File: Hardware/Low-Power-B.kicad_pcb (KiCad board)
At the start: 2 copper layers, 55.2 x 40.6 mm, 25 parts, among them J1 01x02, Q1 BC557, Q2 BC547, Q3 BC557, Q4 BC547, Q5 BC547, U1 Arduino_Pro_Micro, U2 VS1838B

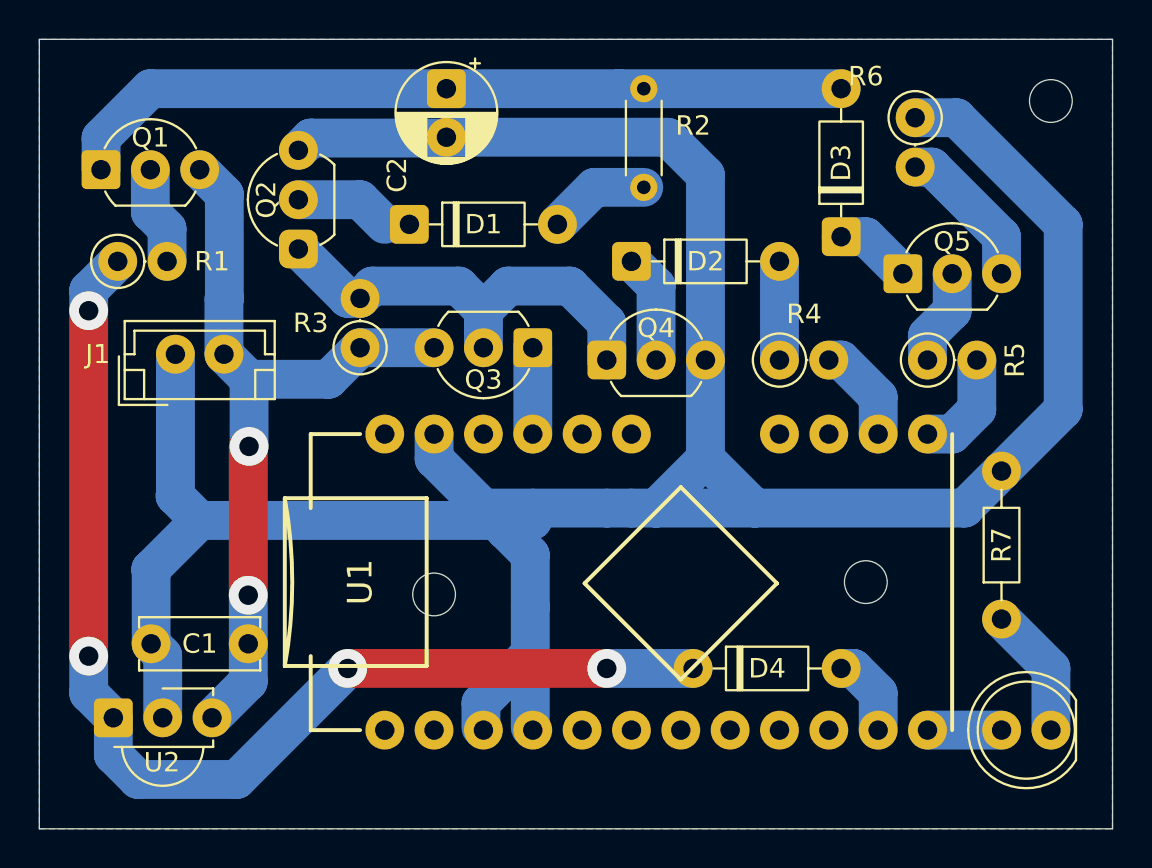
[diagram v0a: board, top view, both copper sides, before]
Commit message: Adding Low-Power-B 3D model
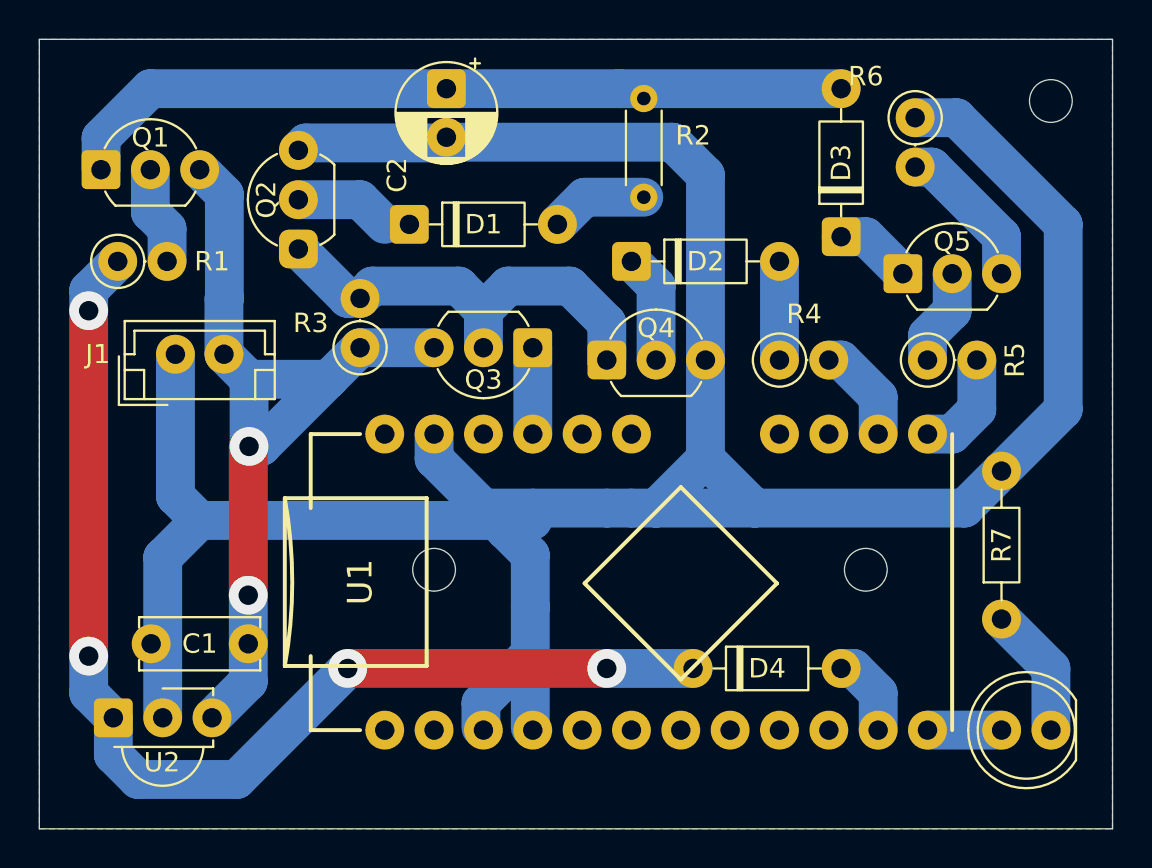
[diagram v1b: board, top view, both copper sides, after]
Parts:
- moved H2 1.27 mm to (162.6, 78.1)
- moved H3 0.63 mm to (184.8, 78.1)
- moved R2 0.51 mm to (173.4, 58.9)
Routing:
- net +5V: track 40.3 -> 45.8 mm
- net GND: track 154.8 -> 153.9 mm
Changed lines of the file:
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@@
 	(footprint "MountingHole:MountingHole_2.2mm_M2_ISO7380"
 		(layer "F.Cu")
-		(at 184.785 78.74)
+		(at 184.785 78.105)
 		(descr "Mounting Hole 2.2mm, M2, no annular, generated by kicad-footprint-generator mountinghole.py")
 		(tags "mountinghole M2 ISO7380")
@@
 	(footprint "Resistor_THT:R_Axial_DIN0204_L3.6mm_D1.6mm_P5.08mm_Horizontal"
 		(layer "F.Cu")
-		(at 173.355 58.42 90)
+		(at 173.355 58.928 90)
 		(descr "Resistor, Axial_DIN0204 series, Axial, Horizontal, pin pitch=5.08mm, 0.167W, length*diameter=3.6*1.6mm^2, http://cdn-reichelt.de/documents/datenblatt/B400/1_4W%23YAG.pdf")
 		(tags "Resistor Axial_DIN0204 series Axial Horizontal pin pitch 5.08mm 0.167W length 3.6mm diameter 1.6mm")
@@
 	(footprint "MountingHole:MountingHole_2.2mm_M2_ISO7380"
 		(layer "F.Cu")
-		(at 162.56 79.375)
+		(at 162.56 78.105)
 		(descr "Mounting Hole 2.2mm, M2, no annular, generated by kicad-footprint-generator mountinghole.py")
 		(tags "mountinghole M2 ISO7380")
@@
 	)
 	(segment
-		(start 147.995 81.915)
-		(end 147.995 78.105)
+		(start 163.195 56.094)
+		(end 174.839 56.094)
+		(width 2)
+		(layer "B.Cu")
+		(net 1)
+	)
+	(segment
+		(start 148.59 77.47)
+		(end 150.495 75.565)
+		(width 2)
+		(layer "B.Cu")
+		(net 1)
+	)
+	(segment
+		(start 148.59 85.725)
+		(end 148.59 77.47)
 		(width 2)
 		(layer "B.Cu")
@@
 	)
 	(segment
-		(start 148.59 85.725)
-		(end 148.59 82.51)
-		(width 2)
-		(layer "B.Cu")
-		(net 1)
-	)
-	(segment
-		(start 150.475 75.545)
-		(end 149.225 74.295)
+		(start 149.245 74.315)
+		(end 150.495 75.565)
 		(width 2)
 		(layer "B.Cu")
@@
 	)
 	(segment
-		(start 148.59 82.51)
-		(end 147.995 81.915)
+		(start 149.245 67.01)
+		(end 149.245 74.315)
 		(width 2)
 		(layer "B.Cu")
@@
 	)
 	(segment
-		(start 149.225 74.295)
-		(end 149.245 74.275)
-		(width 2)
-		(layer "B.Cu")
-		(net 1)
-	)
-	(segment
 		(start 164.973 84.963)
 		(end 167.513 82.423)
@@
 	)
 	(segment
-		(start 163.195 55.84)
-		(end 174.585 55.84)
-		(width 2)
-		(layer "B.Cu")
-		(net 1)
-	)
-	(segment
-		(start 156.21 55.88)
-		(end 155.575 56.515)
-		(width 2)
-		(layer "B.Cu")
-		(net 1)
-	)
-	(segment
 		(start 176.53 67.31)
 		(end 176.53 72.39)
@@
 	)
 	(segment
-		(start 147.975 78.085)
-		(end 150.475 75.585)
-		(width 2)
-		(layer "B.Cu")
-		(net 1)
-	)
-	(segment
 		(start 189.455 54.835)
 		(end 194.945 60.325)
@@
 	)
 	(segment
+		(start 167.64 74.93)
+		(end 165.1 74.93)
+		(width 2)
+		(layer "B.Cu")
+		(net 1)
+	)
+	(segment
+		(start 166.243 76.073)
+		(end 167.513 77.343)
+		(width 2)
+		(layer "B.Cu")
+		(net 1)
+	)
+	(segment
+		(start 155.575 56.515)
+		(end 155.956 56.134)
+		(width 2)
+		(layer "B.Cu")
+		(net 1)
+	)
+	(segment
+		(start 176.53 72.39)
+		(end 179.07 74.93)
+		(width 2)
+		(layer "B.Cu")
+		(net 1)
+	)
+	(segment
+		(start 174.839 56.094)
+		(end 176.53 57.785)
+		(width 2)
+		(layer "B.Cu")
+		(net 1)
+	)
+	(segment
+		(start 171.45 74.93)
+		(end 167.64 74.93)
+		(width 2)
+		(layer "B.Cu")
+		(net 1)
+	)
+	(segment
+		(start 162.56 72.39)
+		(end 165.1 74.93)
+		(width 2)
+		(layer "B.Cu")
+		(net 1)
+	)
+	(segment
+		(start 162.916113 56.134)
+		(end 155.956 56.134)
+		(width 2)
+		(layer "B.Cu")
+		(net 1)
+	)
+	(segment
+		(start 194.945 60.325)
+		(end 194.945 69.85)
+		(width 2)
+		(layer "B.Cu")
+		(net 1)
+	)
+	(segment
+		(start 189.865 74.93)
+		(end 191.77 73.025)
+		(width 2)
+		(layer "B.Cu")
+		(net 1)
+	)
+	(segment
+		(start 173.99 74.93)
+		(end 179.07 74.93)
+		(width 2)
+		(layer "B.Cu")
+		(net 1)
+	)
+	(segment
+		(start 162.56 71.12)
+		(end 162.56 72.39)
+		(width 2)
+		(layer "B.Cu")
+		(net 1)
+	)
+	(segment
 		(start 176.53 57.785)
 		(end 176.53 67.31)
-		(width 2)
-		(layer "B.Cu")
-		(net 1)
-	)
-	(segment
-		(start 167.64 74.93)
-		(end 165.1 74.93)
-		(width 2)
-		(layer "B.Cu")
-		(net 1)
-	)
-	(segment
-		(start 166.243 76.073)
-		(end 167.513 77.343)
-		(width 2)
-		(layer "B.Cu")
-		(net 1)
-	)
-	(segment
-		(start 176.53 72.39)
-		(end 179.07 74.93)
-		(width 2)
-		(layer "B.Cu")
-		(net 1)
-	)
-	(segment
-		(start 147.995 78.105)
-		(end 147.975 78.085)
-		(width 2)
-		(layer "B.Cu")
-		(net 1)
-	)
-	(segment
-		(start 171.45 74.93)
-		(end 167.64 74.93)
-		(width 2)
-		(layer "B.Cu")
-		(net 1)
-	)
-	(segment
-		(start 162.56 72.39)
-		(end 165.1 74.93)
-		(width 2)
-		(layer "B.Cu")
-		(net 1)
-	)
-	(segment
-		(start 163.170113 55.88)
-		(end 156.21 55.88)
-		(width 2)
-		(layer "B.Cu")
-		(net 1)
-	)
-	(segment
-		(start 149.245 74.275)
-		(end 149.245 67.01)
-		(width 2)
-		(layer "B.Cu")
-		(net 1)
-	)
-	(segment
-		(start 194.945 60.325)
-		(end 194.945 69.85)
-		(width 2)
-		(layer "B.Cu")
-		(net 1)
-	)
-	(segment
-		(start 189.865 74.93)
-		(end 191.77 73.025)
-		(width 2)
-		(layer "B.Cu")
-		(net 1)
-	)
-	(segment
-		(start 174.585 55.84)
-		(end 176.53 57.785)
-		(width 2)
-		(layer "B.Cu")
-		(net 1)
-	)
-	(segment
-		(start 173.99 74.93)
-		(end 179.07 74.93)
-		(width 2)
-		(layer "B.Cu")
-		(net 1)
-	)
-	(segment
-		(start 162.56 71.12)
-		(end 162.56 72.39)
 		(width 2)
 		(layer "B.Cu")
@@
 	)
 	(segment
-		(start 170.815 58.42)
-		(end 168.91 60.325)
+		(start 153.67 71.755)
+		(end 157.125 68.3)
+		(width 2)
+		(layer "B.Cu")
+		(net 2)
+	)
+	(segment
+		(start 153.035 71.755)
+		(end 153.67 71.755)
+		(width 2)
+		(layer "B.Cu")
+		(net 2)
+	)
+	(segment
+		(start 168.91 60.325)
+		(end 170.307 58.928)
 		(width 2)
 		(layer "B.Cu")
@@
 	)
 	(segment
-		(start 173.355 58.42)
-		(end 170.815 58.42)
-		(width 2)
-		(layer "B.Cu")
+		(start 170.307 58.928)
+		(end 173.355 58.928)
+		(width 2)
+		(layer "B.Cu")

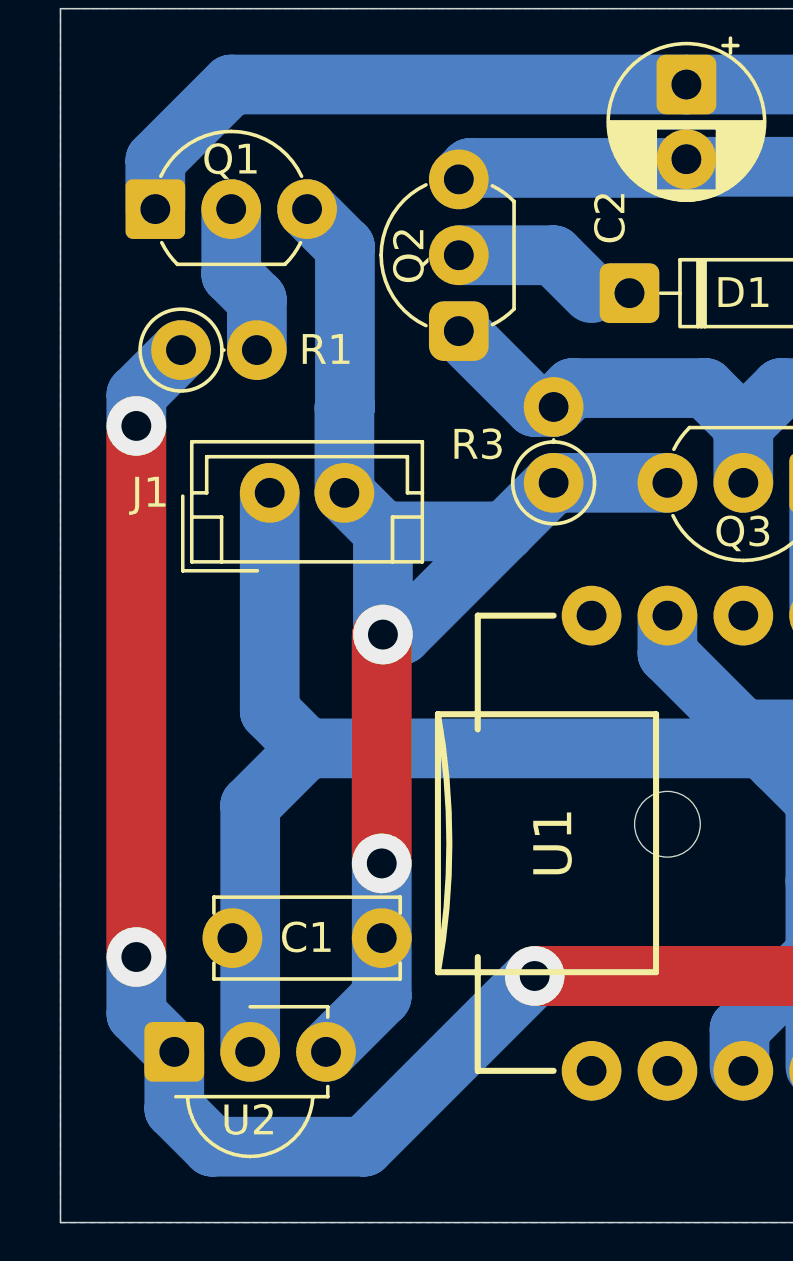
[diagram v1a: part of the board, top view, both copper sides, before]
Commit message: Minor fixes on Low-Power-B 3D model
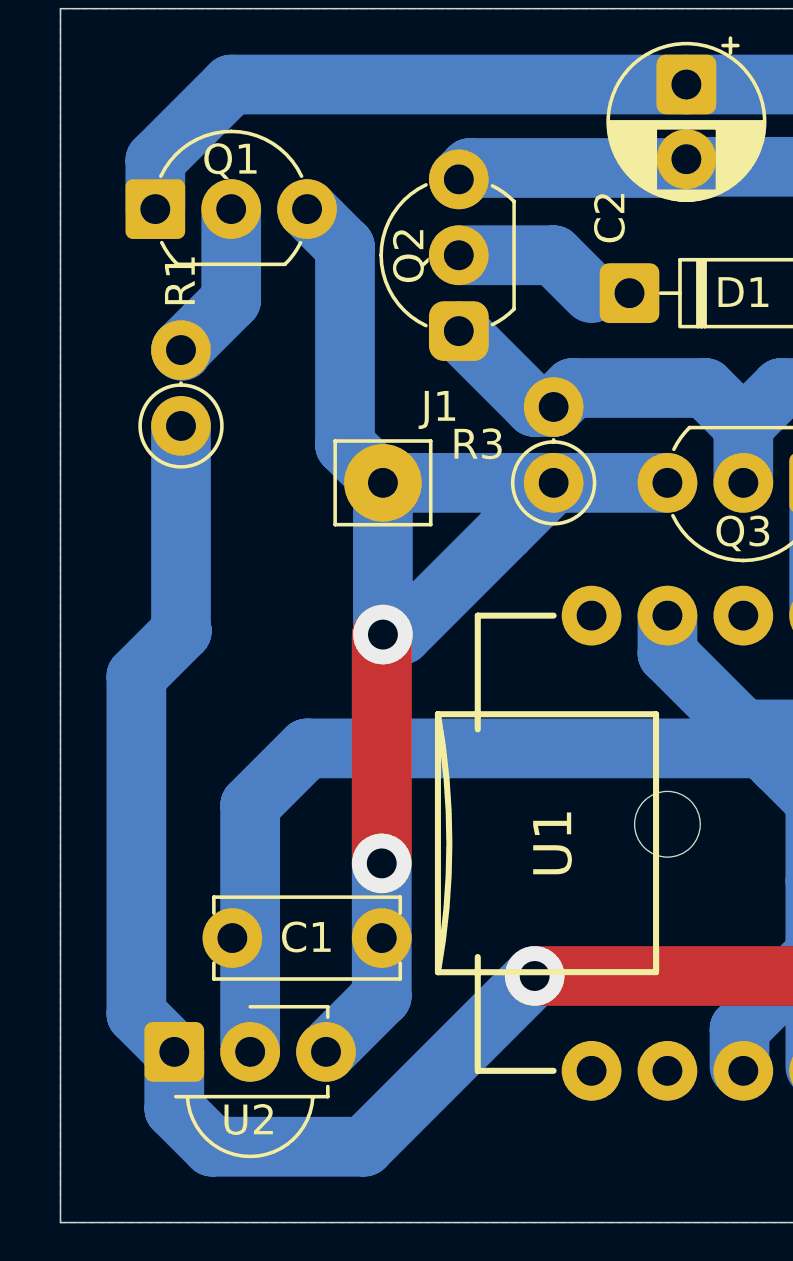
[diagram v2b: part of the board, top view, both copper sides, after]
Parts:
- J1: value 01x02 -> USB; footprint Connector_JST:JST_EH_B2B-EH-A_1x02_P2.50mm_Vertical -> Connector_Pin:Pin_D1.2mm_L11.3mm_W3.0mm_Flat
- R5, R6: value 4.7K -> 4K7
- R7: value 1K -> 4K7
- moved J1 3.80 mm to (153.0, 66.7)
- moved R1 2.54 mm to (146.3, 64.8), turned to 90 degrees
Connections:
- J1 pad 1: GND -> +5V
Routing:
- net GND: track 153.9 -> 144.8 mm
- net IR_OUT: track 59.3 -> 56.8 mm, vias 4 -> 2
- net +5V: track 45.8 -> 47.4 mm

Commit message: update README.md
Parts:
- removed H3: MountingHole, MountingHole:MountingHole_2.2mm_M2_ISO7380
- J1: value USB -> USB_VBUS; footprint Connector_Pin:Pin_D1.2mm_L11.3mm_W3.0mm_Flat -> Connector_JST:JST_EH_B2B-EH-A_1x02_P2.50mm_Vertical
- R2: footprint Resistor_THT:R_Axial_DIN0204_L3.6mm_D1.6mm_P5.08mm_Horizontal -> Resistor_THT:R_Axial_DIN0207_L6.3mm_D2.5mm_P7.62mm_Horizontal
- moved H2 17.1 mm to (179.7, 78.1)
- moved D3 7.10 mm to (184.8, 54.0), turned to 180 degrees
- moved D2 3.18 mm to (175.9, 62.2)
- moved Q3 2.54 mm to (170.2, 66.7)
- moved Q4 2.54 mm to (174.0, 67.3)
- moved R3 2.54 mm to (161.3, 66.7)
- moved R4 2.54 mm to (182.9, 67.3)
- moved R6 2.01 mm to (189.2, 55.5)
- moved J1 1.88 mm to (154.9, 66.7), turned to 180 degrees
- moved R2 1.53 mm to (172.7, 60.3)
- moved R5 1.27 mm to (189.2, 67.3)
- moved C1 0.67 mm to (148.7, 81.9)
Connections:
- net +5V renamed VBUS
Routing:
- net VCC: track 4.45 -> 33.0 mm, vias 0 -> 2
- net Net-(D3-A): track 40.8 -> 34.7 mm
- net Net-(D3-K): track 3.96 -> 9.68 mm
- net GND: track 144.8 -> 141.2 mm, vias 0 -> 2
- net Net-(Q2-C): track 22.8 -> 25.4 mm
- net Net-(Q5-E): track 7.83 -> 5.91 mm
- net ON_OFF: track 5.23 -> 3.81 mm
- net Net-(D1-A): track 5.02 -> 3.81 mm
- net VBUS: track 47.4 -> 48.3 mm, vias 2 -> 0
- net DISCH: track 5.61 -> 6.13 mm
- net Net-(Q5-B): track 4.97 -> 4.45 mm
